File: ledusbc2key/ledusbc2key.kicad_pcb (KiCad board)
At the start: 2 copper layers, 24 parts, among them SW1 SW_Push, U1 ATmega32U2-A, U2 PRTR5V0U2X, Y1 Crystal_GND24_Small

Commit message: finished 2k
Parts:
- removed MX3: MX-NoLED, MX_Alps_Hybrid:MX-1U-NoLED
- added ?: , , F.Cu at (146.7, 64.8)
- added MX1: MX-NoLED, MX_Only:MXOnly-1U-Hotswap, F.Cu at (137.2, 79.4)
- added REF**: MountingHole_2.1mm, MountingHole:MountingHole_2.1mm, F.Cu at (108.6, 64.8)
- added REF**: MountingHole_2.1mm, MountingHole:MountingHole_2.1mm, F.Cu at (146.7, 64.8)
- added REF**: MountingHole_2.1mm, MountingHole:MountingHole_2.1mm, F.Cu at (146.7, 110.2)
- added REF**: MountingHole_2.1mm, MountingHole:MountingHole_2.1mm, F.Cu at (108.6, 110.2)
- C1, C2, C3, C4, C5, C6, C7, C8, D1, D2, F1, R1, R2, R3, R4, R5, R6, SW1, U1, U2, USB1, Y1: moved to B.Cu
- MX2: footprint MX_Alps_Hybrid:MX-1U-NoLED -> MX_Only:MXOnly-1U-Hotswap
- moved Y1 49.1 mm to (135.3, 105.7), turned to 45 degrees
- moved USB1 42.3 mm to (127.6, 57.6)
- moved C8 39.5 mm to (136.4, 96.9), turned to 45 degrees
- moved R4 36.2 mm to (123.8, 70.2), turned to 90 degrees
- moved F1 35.9 mm to (136.5, 67.3), turned to 180 degrees
- moved U2 33.6 mm to (127.6, 71.1)
- moved R5 29.2 mm to (131.4, 70.2), turned to 90 degrees
- moved C6 27.3 mm to (136.3, 71.1), turned to 180 degrees
- moved R6 26.4 mm to (122.9, 105.4), turned to -45 degrees
- moved D2 25.7 mm to (140.3, 87.6), turned to 180 degrees
- moved C5 25.1 mm to (110.2, 87.6), turned to 90 degrees
- moved R2 23.3 mm to (133.1, 93.0), turned to -135 degrees
- moved D1 19.9 mm to (114.9, 87.6)
- moved R1 19.7 mm to (119.4, 96.2), turned to -90 degrees
- moved R3 17.2 mm to (134.7, 94.5), turned to 45 degrees
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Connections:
- U1 pad 16: COL0 -> unconnected-(U1-Pad16)
- U1 pad 17: COL1 -> LED
- U1 pad 23: LED -> unconnected-(U1-Pad23)
- U1 pad 25: unconnected-(U1-Pad25) -> COL1
- U1 pad 26: unconnected-(U1-Pad26) -> COL0
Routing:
- net +5V: track 0.00 -> 106.6 mm, vias 0 -> 4
- net GND: track 0.00 -> 91.8 mm
- net D-: track 0.00 -> 38.3 mm, vias 0 -> 2
- net D+: track 0.00 -> 34.2 mm
- net COL0: track 0.00 -> 30.0 mm, vias 0 -> 2
- net COL1: track 0.00 -> 28.3 mm
- net Net-(D1-Pad2): track 0.00 -> 26.5 mm, vias 0 -> 2
- net VCC: track 0.00 -> 20.9 mm, vias 0 -> 3
- net LED: track 0.00 -> 18.6 mm, vias 0 -> 2
- net Net-(R1-Pad2): track 0.00 -> 13.5 mm
- net XTAL2: track 0.00 -> 13.2 mm
- net XTAL1: track 0.00 -> 10.4 mm, vias 0 -> 2
- net Net-(R4-Pad2): track 0.00 -> 5.42 mm
- net Net-(C1-Pad1): track 0.00 -> 4.46 mm
- net Net-(R5-Pad2): track 0.00 -> 4.41 mm
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- added copper zone on B.Cu, net GND
- added copper zone on F.Cu, net GND
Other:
- board outline added: 43.8 x 54.3 mm
- board text added: "alexoltl#8251"

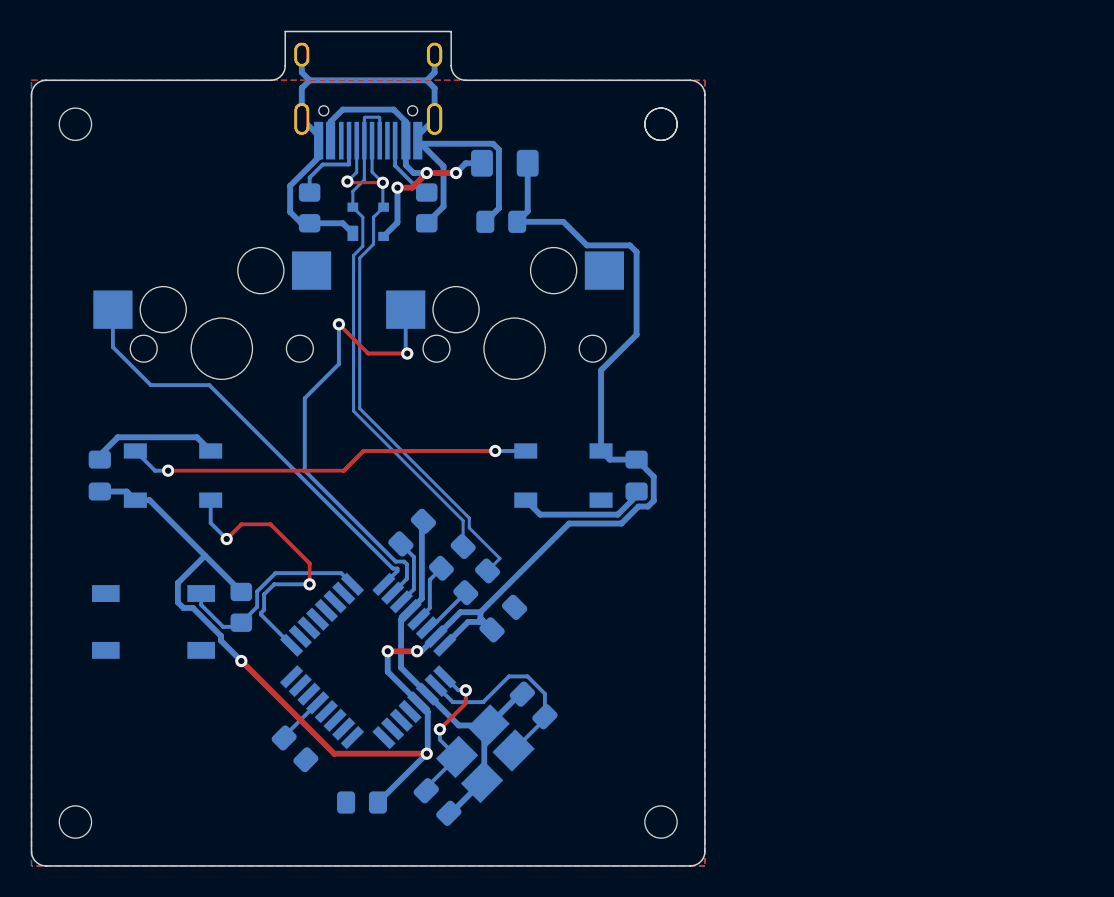
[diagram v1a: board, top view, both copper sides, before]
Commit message: changed location of pcb mountings
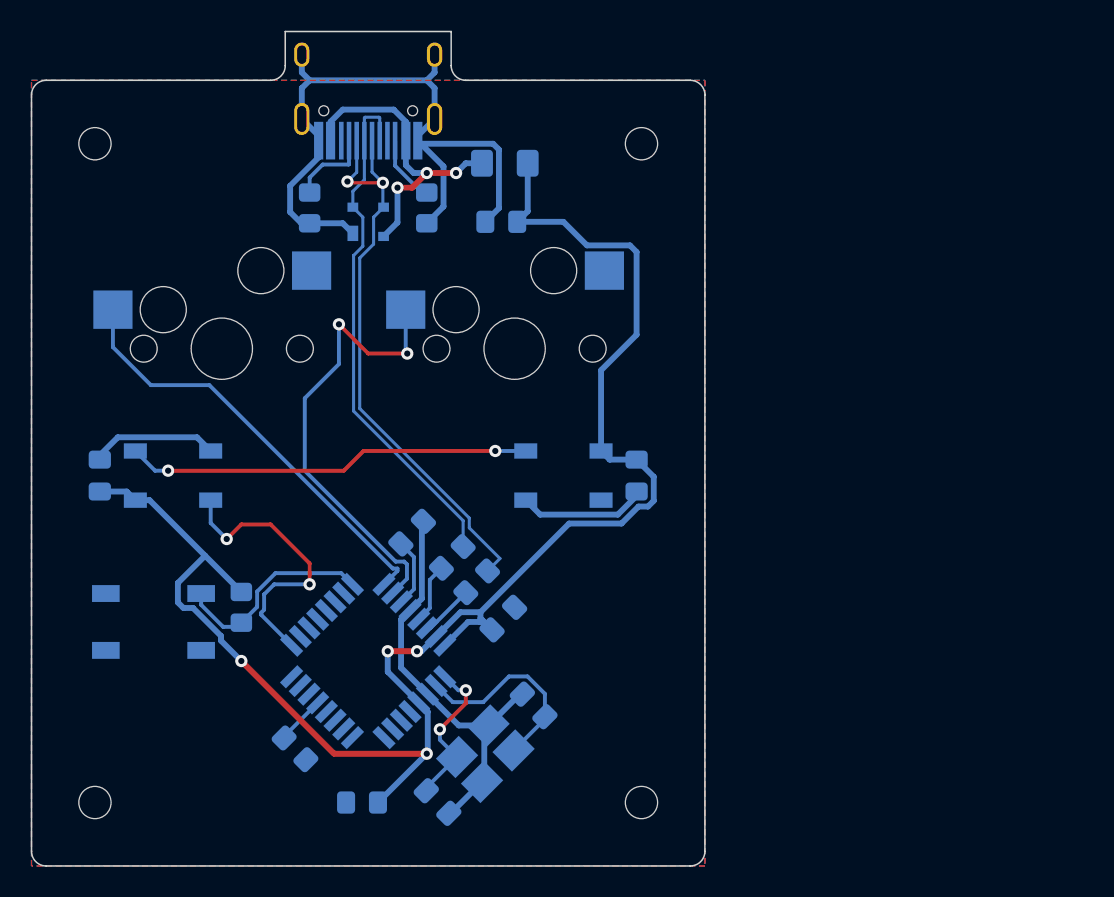
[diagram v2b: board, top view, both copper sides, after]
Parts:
- removed ?: , 
- moved REF** 1.80 mm to (109.9, 66.0)
- moved REF** 1.80 mm to (145.4, 66.0)
- moved REF** 1.80 mm to (145.4, 108.9)
- moved REF** 1.80 mm to (109.9, 108.9)
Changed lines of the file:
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@@
     )
-  )
-  (footprint "" (layer "F.Cu")
-    (at 146.685 64.77)
-    (fp_text reference "" (at 0 0) (layer "F.SilkS")
-      (effects (font (size 1.27 1.27) (thickness 0.15)))
-    )
-    (fp_text value "" (at 0 0) (layer "F.SilkS")
-      (effects (font (size 1.27 1.27) (thickness 0.15)))
-    )
-    (pad "" np_thru_hole circle (at 0 0) (size 2.1 2.1) (drill 2.1) (layers *.Cu *.Mask))
   )
   (footprint "MountingHole:MountingHole_2.1mm" (layer "F.Cu")
-    (at 108.585 64.77)
+    (at 109.855 66.04)
     (descr "Mounting Hole 2.1mm, no annular")
     (tags "mounting hole 2.1mm no annular")
@@
   )
   (footprint "MountingHole:MountingHole_2.1mm" (layer "F.Cu")
-    (at 146.685 64.77)
+    (at 145.415 66.04)
     (descr "Mounting Hole 2.1mm, no annular")
     (tags "mounting hole 2.1mm no annular")
@@
   )
   (footprint "MountingHole:MountingHole_2.1mm" (layer "F.Cu")
-    (at 146.685 110.1725)
+    (at 145.415 108.9025)
     (descr "Mounting Hole 2.1mm, no annular")
     (tags "mounting hole 2.1mm no annular")
@@
   )
   (footprint "MountingHole:MountingHole_2.1mm" (layer "F.Cu")
-    (at 108.585 110.1725)
+    (at 109.855 108.9025)
     (descr "Mounting Hole 2.1mm, no annular")
     (tags "mounting hole 2.1mm no annular")
@@
     (property "Sheetname" "")
     (attr smd)
-    (fp_text reference "R4" (at 0 -2.54 90) (layer "B.SilkS")
+    (fp_text reference "R4" (at 0.365 -2.2225 90) (layer "B.SilkS")
       (effects (font (size 1 1) (thickness 0.15)) (justify mirror))
     )
@@
     (property "Sheetname" "")
     (attr smd)
-    (fp_text reference "R5" (at 0 2.54 90) (layer "B.SilkS")
+    (fp_text reference "R5" (at 0.0475 1.905 90) (layer "B.SilkS")
       (effects (font (size 1 1) (thickness 0.15)) (justify mirror))
     )
@@
     (property "Sheetname" "")
     (attr smd)
-    (fp_text reference "C3" (at -0.224506 -2.963711 135) (layer "B.SilkS")
+    (fp_text reference "C3" (at 0 -1.841179 135) (layer "B.SilkS")
       (effects (font (size 1 1) (thickness 0.15)) (justify mirror))
     )
@@
     (property "Sheetname" "")
     (attr smd)
-    (fp_text reference "U1" (at 0 6.05 135) (layer "B.SilkS")
+    (fp_text reference "U1" (at 0 6.05 315) (layer "B.SilkS")
       (effects (font (size 1 1) (thickness 0.15)) (justify mirror))
     )
@@
     (property "Sheetname" "")
     (attr smd)
-    (fp_text reference "C2" (at 0.248981 -2.539172 135) (layer "B.SilkS")
+    (fp_text reference "C2" (at 0.024474 -1.865653 135) (layer "B.SilkS")
       (effects (font (size 1 1) (thickness 0.15)) (justify mirror))
     )
@@
     (property "Sheetname" "")
     (attr smd)
-    (fp_text reference "R1" (at 0 1.65 90) (layer "B.SilkS")
+    (fp_text reference "R1" (at 0 -1.905 -90) (layer "B.SilkS")
       (effects (font (size 1 1) (thickness 0.15)) (justify mirror))
     )
@@
     (property "Sheetname" "")
     (attr smd)
-    (fp_text reference "Y1" (at 0.224506 3.367596 45) (layer "B.SilkS")
+    (fp_text reference "Y1" (at 0 3.14309 45) (layer "B.SilkS")
       (effects (font (size 1 1) (thickness 0.15)) (justify mirror))
     )
@@
     (property "Sheetname" "")
     (attr smd)
-    (fp_text reference "C6" (at 0 1.905) (layer "B.SilkS")
+    (fp_text reference "C6" (at 0.085 -1.905) (layer "B.SilkS")
       (effects (font (size 1 1) (thickness 0.15)) (justify mirror))
     )
@@
     (property "Sheetname" "")
     (attr smd)
-    (fp_text reference "C7" (at -0.261252 1.68) (layer "B.SilkS")
+    (fp_text reference "C7" (at -0.085 1.5875) (layer "B.SilkS")
       (effects (font (size 1 1) (thickness 0.15)) (justify mirror))
     )
@@
   )
   (dimension (type aligned) (layer "B.Cu")
-    (pts (xy 149.5425 61.9125) (xy 105.7275 61.9125))
-    (height 8.5725)
-    (gr_text "43.8150 mm" (at 127.635 51.54) (layer "B.Cu")
+    (pts (xy 133.0325 60.96) (xy 149.5425 60.96))
+    (height -13.97)
+    (gr_text "16.5100 mm" (at 141.2875 45.19) (layer "B.Cu")
       (effects (font (size 1.5 1.5) (thickness 0.3)))
     )
+    (format (units 3) (units_format 1) (precision 4))
+    (style (thickness 0.2) (arrow_length 1.27) (text_position_mode 0) (extension_height 0.58642) (extension_offset 0.5) keep_text_aligned)
+  )
+  (dimension (type aligned) (layer "B.Cu")
+    (pts (xy 133.0325 58.7375) (xy 122.2375 58.7375))
+    (height 6.6675)
+    (gr_text "10.7950 mm" (at 127.635 50.27) (layer "B.Cu")
+      (effects (font (size 1.5 1.5) (thickness 0.3)))
+    )
+    (format (units 3) (units_format 1) (precision 4))
+    (style (thickness 0.2) (arrow_length 1.27) (text_position_mode 0) (extension_height 0.58642) (extension_offset 0.5) keep_text_aligned)
+  )
+  (dimension (type aligned) (layer "B.Cu")
+    (pts (xy 149.5425 113.03) (xy 105.7275 113.03))
+    (height -4.1275)
+    (gr_text "43.8150 mm" (at 127.635 115.3575) (layer "B.Cu")
+      (effects (font (size 1.5 1.5) (thickness 0.3)))
+    )
